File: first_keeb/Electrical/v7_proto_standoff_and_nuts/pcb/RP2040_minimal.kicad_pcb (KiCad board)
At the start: 2 copper layers, 77.7 x 77.5 mm, 71 parts, among them P1 USB-TYPE-C-016, Q1 SN74LV1T34DBV, SW1 SKRKAGE020, SW2 PTS647 SN70 SMTR2 LFS, SW3 PTS647 SN70 SMTR2 LFS, U1 NCP1117-3.3_SOT223, U2 LM4040DBZ-3, U3 PRTR5V0U2X, U4 W25Q32JVSS, U5 RP2040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

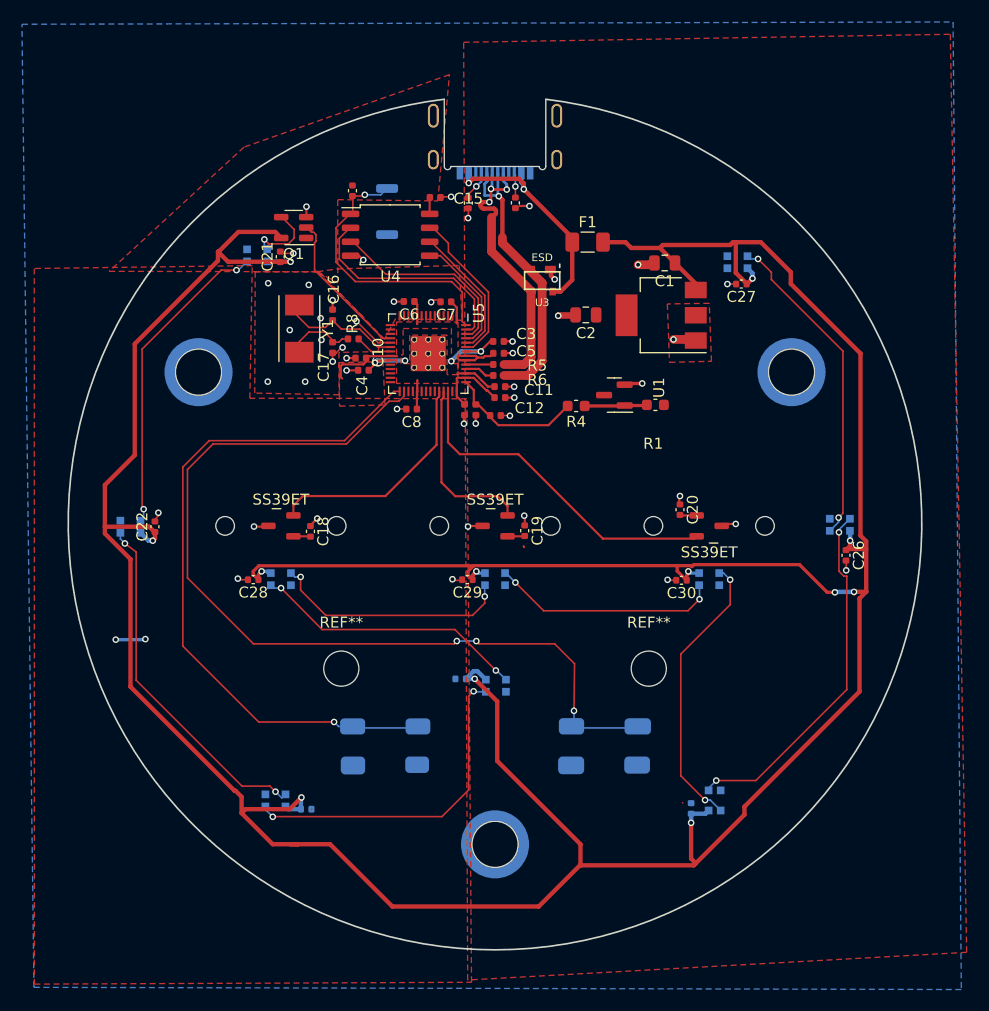
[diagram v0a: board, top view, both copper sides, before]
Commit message: adds another option for pcb with threaded insert
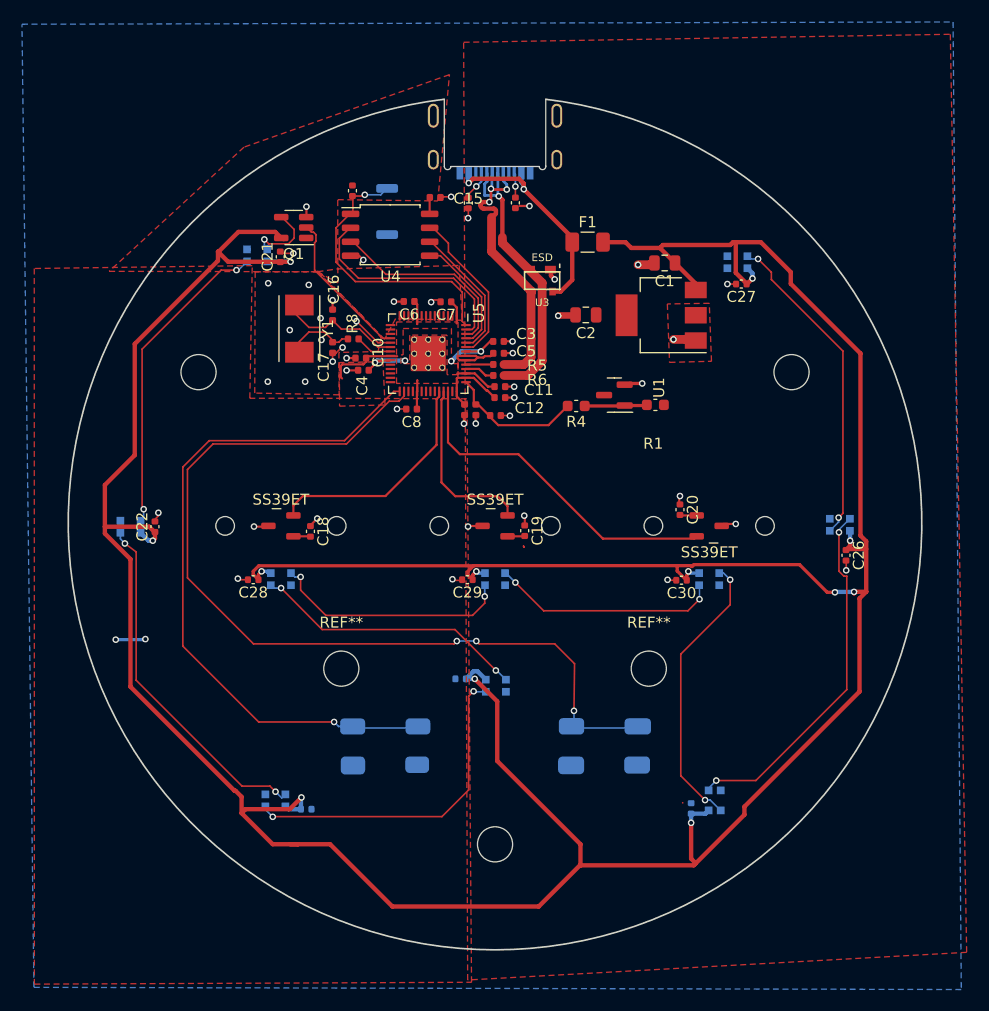
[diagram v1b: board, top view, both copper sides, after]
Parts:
- H1, H2, H3: value M3_Threaded_Insert_4881_Keystone -> MountingHole_3.2mm_M3; footprint MountingHole:M3_Threaded_Insert_4881_Keystone -> MountingHole:MountingHole_3.2mm_M3
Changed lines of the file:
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@@
     )
   )
-  (footprint "MountingHole:M3_Threaded_Insert_4881_Keystone" (layer "B.Cu")
+  (footprint "MountingHole:MountingHole_3.2mm_M3" (layer "B.Cu")
     (at 100 129 180)
+    (descr "Mounting Hole 3.2mm, no annular, M3")
+    (tags "mounting hole 3.2mm no annular m3")
     (property "Sheetfile" "RP2040_minimal.kicad_sch")
     (property "Sheetname" "")
     (property "ki_description" "Mounting Hole with connection")
     (property "ki_keywords" "mounting hole")
-    (attr smd)
-    (fp_text reference "H3" (at 0 0.5 unlocked) (layer "B.SilkS")
-        (effects (font (size 1 1) (thickness 0.15)) (justify mirror))
-    )
-    (fp_text value "M3_Threaded_Insert_4881_Keystone" (at 0 -1 unlocked) (layer "B.Fab")
-        (effects (font (size 1 1) (thickness 0.15)) (justify mirror))
-    )
-    (fp_text user "${REFERENCE}" (at 0 -2.5 unlocked) (layer "B.Fab")
+    (attr exclude_from_pos_files exclude_from_bom)
+    (fp_text reference "H3" (at 0 4.2) (layer "B.SilkS")
+        (effects (font (size 1 1) (thickness 0.15)) (justify mirror))
+    )
+    (fp_text value "MountingHole_3.2mm_M3" (at 0 -4.2) (layer "B.Fab")
+        (effects (font (size 1 1) (thickness 0.15)) (justify mirror))
+    )
+    (fp_text user "${REFERENCE}" (at 0 0) (layer "B.Fab")
         (effects (font (size 1 1) (thickness 0.15)) (justify mirror))
     )
     (fp_circle (center 0 0) (end 3.2 0)
-      (stroke (width 0.12) (type default)) (fill none) (layer "Cmts.User"))
-    (pad "" np_thru_hole circle (at 0 0 180) (size 4.2 4.2) (drill 4.2) (layers "F&B.Cu" "*.Mask"))
-    (pad "1" smd circle (at 0 0 180) (size 6.2 6.2) (layers "B.Cu" "B.Mask"))
+      (stroke (width 0.15) (type solid)) (fill none) (layer "Cmts.User"))
+    (fp_circle (center 0 0) (end 3.45 0)
+      (stroke (width 0.05) (type solid)) (fill none) (layer "B.CrtYd"))
+    (pad "" np_thru_hole circle (at 0 0 180) (size 3.2 3.2) (drill 3.2) (layers "*.Cu" "*.Mask"))
   )
   (footprint "Button_Switch_SMD:PTS647_4.5x4.5mm" (layer "B.Cu")
@@
     )
   )
-  (footprint "MountingHole:M3_Threaded_Insert_4881_Keystone" (layer "B.Cu")
+  (footprint "MountingHole:MountingHole_3.2mm_M3" (layer "B.Cu")
     (at 73 86 180)
+    (descr "Mounting Hole 3.2mm, no annular, M3")
+    (tags "mounting hole 3.2mm no annular m3")
     (property "Sheetfile" "RP2040_minimal.kicad_sch")
     (property "Sheetname" "")
     (property "ki_description" "Mounting Hole with connection")
     (property "ki_keywords" "mounting hole")
-    (attr smd)
-    (fp_text reference "H2" (at 0 0.5 unlocked) (layer "B.SilkS")
-        (effects (font (size 1 1) (thickness 0.15)) (justify mirror))
-    )
-    (fp_text value "M3_Threaded_Insert_4881_Keystone" (at 0 -1 unlocked) (layer "B.Fab")
-        (effects (font (size 1 1) (thickness 0.15)) (justify mirror))
-    )
-    (fp_text user "${REFERENCE}" (at 0 -2.5 unlocked) (layer "B.Fab")
+    (attr exclude_from_pos_files exclude_from_bom)
+    (fp_text reference "H2" (at 0 4.2) (layer "B.SilkS")
+        (effects (font (size 1 1) (thickness 0.15)) (justify mirror))
+    )
+    (fp_text value "MountingHole_3.2mm_M3" (at 0 -4.2) (layer "B.Fab")
+        (effects (font (size 1 1) (thickness 0.15)) (justify mirror))
+    )
+    (fp_text user "${REFERENCE}" (at 0 0) (layer "B.Fab")
         (effects (font (size 1 1) (thickness 0.15)) (justify mirror))
     )
     (fp_circle (center 0 0) (end 3.2 0)
-      (stroke (width 0.12) (type default)) (fill none) (layer "Cmts.User"))
-    (pad "" np_thru_hole circle (at 0 0 180) (size 4.2 4.2) (drill 4.2) (layers "F&B.Cu" "*.Mask"))
-    (pad "1" smd circle (at 0 0 180) (size 6.2 6.2) (layers "B.Cu" "B.Mask"))
+      (stroke (width 0.15) (type solid)) (fill none) (layer "Cmts.User"))
+    (fp_circle (center 0 0) (end 3.45 0)
+      (stroke (width 0.05) (type solid)) (fill none) (layer "B.CrtYd"))
+    (pad "" np_thru_hole circle (at 0 0 180) (size 3.2 3.2) (drill 3.2) (layers "*.Cu" "*.Mask"))
   )
   (footprint "Capacitor_SMD:C_0402_1005Metric" (layer "B.Cu")
@@
     )
   )
-  (footprint "MountingHole:M3_Threaded_Insert_4881_Keystone" (layer "B.Cu")
+  (footprint "MountingHole:MountingHole_3.2mm_M3" (layer "B.Cu")
     (at 127 86 180)
+    (descr "Mounting Hole 3.2mm, no annular, M3")
+    (tags "mounting hole 3.2mm no annular m3")
     (property "Sheetfile" "RP2040_minimal.kicad_sch")
     (property "Sheetname" "")
     (property "ki_description" "Mounting Hole with connection")
     (property "ki_keywords" "mounting hole")
-    (attr smd)
-    (fp_text reference "H1" (at 0 0.5 unlocked) (layer "B.SilkS")
-        (effects (font (size 1 1) (thickness 0.15)) (justify mirror))
-    )
-    (fp_text value "M3_Threaded_Insert_4881_Keystone" (at 0 -1 unlocked) (layer "B.Fab")
-        (effects (font (size 1 1) (thickness 0.15)) (justify mirror))
-    )
-    (fp_text user "${REFERENCE}" (at 0 -2.5 unlocked) (layer "B.Fab")
+    (attr exclude_from_pos_files exclude_from_bom)
+    (fp_text reference "H1" (at 0 4.2) (layer "B.SilkS")
+        (effects (font (size 1 1) (thickness 0.15)) (justify mirror))
+    )
+    (fp_text value "MountingHole_3.2mm_M3" (at 0 -4.2) (layer "B.Fab")
+        (effects (font (size 1 1) (thickness 0.15)) (justify mirror))
+    )
+    (fp_text user "${REFERENCE}" (at 0 0) (layer "B.Fab")
         (effects (font (size 1 1) (thickness 0.15)) (justify mirror))
     )
     (fp_circle (center 0 0) (end 3.2 0)
-      (stroke (width 0.12) (type default)) (fill none) (layer "Cmts.User"))
-    (pad "" np_thru_hole circle (at 0 0 180) (size 4.2 4.2) (drill 4.2) (layers "F&B.Cu" "*.Mask"))
-    (pad "1" smd circle (at 0 0 180) (size 6.2 6.2) (layers "B.Cu" "B.Mask"))
+      (stroke (width 0.15) (type solid)) (fill none) (layer "Cmts.User"))
+    (fp_circle (center 0 0) (end 3.45 0)
+      (stroke (width 0.05) (type solid)) (fill none) (layer "B.CrtYd"))
+    (pad "" np_thru_hole circle (at 0 0 180) (size 3.2 3.2) (drill 3.2) (layers "*.Cu" "*.Mask"))
   )
   (footprint "LED_SMD:LED_WS2812B-2020_PLCC4_2.0x2.0mm" (layer "B.Cu")
@@
   (segment (start 118.1 130.91) (end 107.83 130.91) (width 0.4) (layer "F.Cu") (net 36))
   (segment (start 118.28 130.73) (end 118.1 130.91) (width 0.4) (layer "F.Cu") (net 36))
-  (segment (start 83.312 125.818) (end 83.302 125.828) (width 0.15) (layer "F.Cu") (net 36))
   (segment (start 64.47 100.076) (end 64.47 96.28) (width 0.4) (layer "F.Cu") (net 36))
   (segment (start 68.989035 100.556) (end 69.032 100.556) (width 0.4) (layer "F.Cu") (net 36))

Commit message: v1 case and pcb complete
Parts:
- removed the REF** at (86.0, 113.0)
- removed the REF** at (114.0, 113.0)
- added H4: MountingHole_4.3mm_M4, MountingHole:MountingHole_4.3mm_M4, B.Cu at (89.0, 114.0)
- added H5: MountingHole_4.3mm_M4, MountingHole:MountingHole_4.3mm_M4, B.Cu at (111.0, 114.0)
- C21, C22, C26, C27, C28, C29, C30: moved to B.Cu
- moved Q1 2.06 mm to (81.6, 74.9)
- moved R7 1.70 mm to (88.6, 70.1), turned to 180 degrees
- moved SW1 0.61 mm to (90.5, 71.9)
- moved C30 0.06 mm to (116.9, 105.0)
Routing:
- net GND: track 40.9 -> 33.1 mm, vias 46 -> 39
- net LED_D_5V: track 6.68 -> 2.07 mm
- net +5V: track 335.1 -> 331.2 mm
- net LED_D_3V: track 13.7 -> 11.6 mm
- net GPIO18: track 65.0 -> 64.1 mm
- net /QSPI_SD2: track 18.5 -> 17.8 mm
- net /USB_D+: track 25.9 -> 25.7 mm, vias 3 -> 2

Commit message: case with mid mount
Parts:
- P1: moved to F.Cu
- turned P1 to 180 degrees
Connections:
- R2 pad 1: Net-(P1-CC2) -> Net-(P1-CC1)
- R3 pad 1: Net-(P1-CC1) -> Net-(P1-CC2)
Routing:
- net GND: track 33.1 -> 37.3 mm, vias 39 -> 43
- net /USB_D-: track 26.3 -> 25.6 mm, vias 1 -> 2
- net /USB_D+: track 25.7 -> 26.0 mm, vias 2 -> 0
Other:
- board size 77.7 x 77.5 mm -> 77.4 x 77.1 mm
